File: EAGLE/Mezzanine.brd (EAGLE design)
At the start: 83 x 74 mm, 11 parts, among them U1 QBA-07+, U2 QBA-07+, U3 QBA-07+

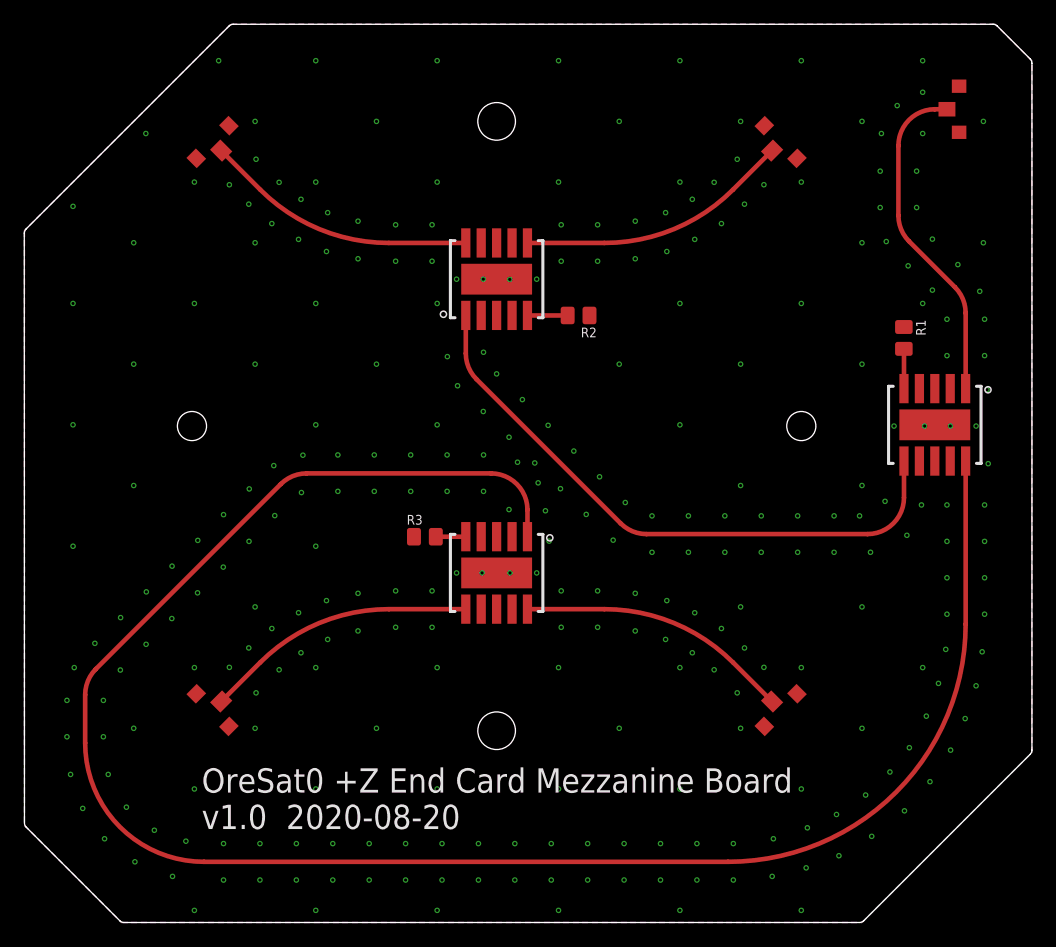
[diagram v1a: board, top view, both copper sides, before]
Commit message: Update mezzanine board to slide in past nubs
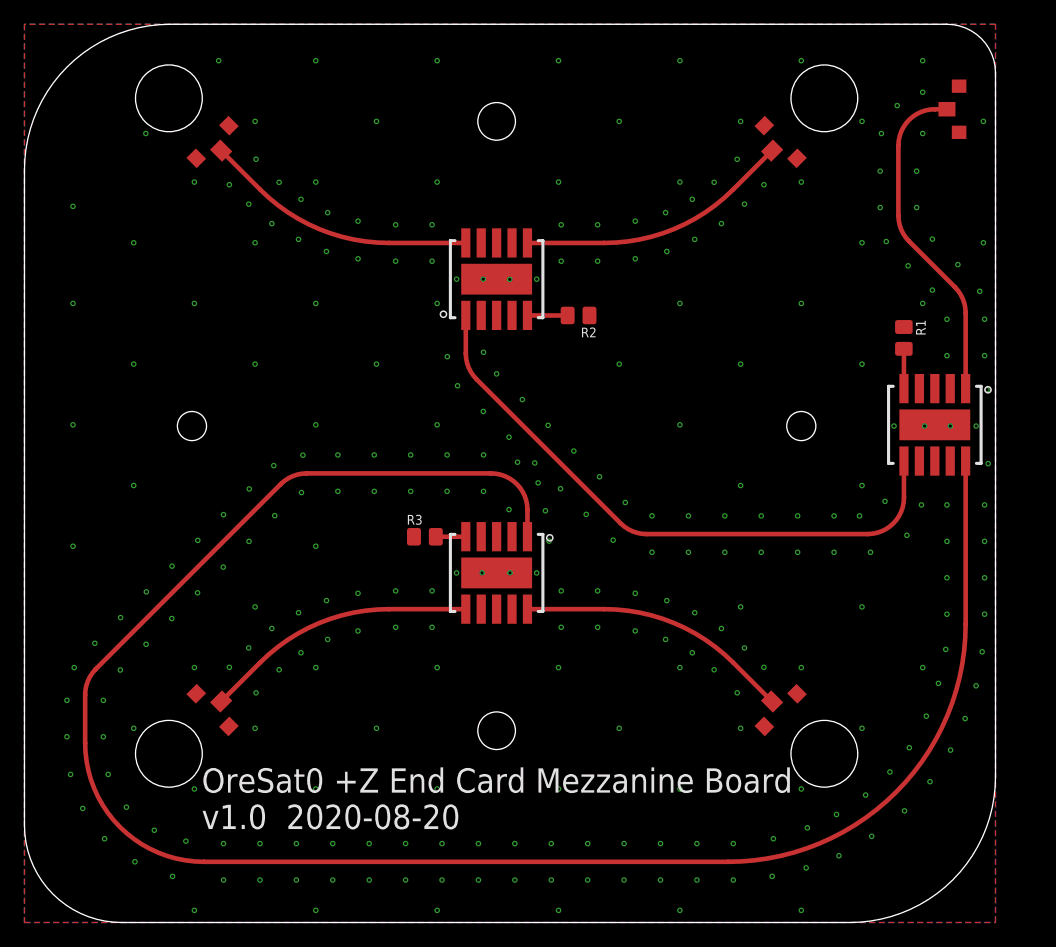
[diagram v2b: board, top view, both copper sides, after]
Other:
- board size 83 x 74 mm -> 80 x 74 mm
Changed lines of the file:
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@@
 <?xml version="1.0" encoding="utf-8"?>
 <!DOCTYPE eagle SYSTEM "eagle.dtd">
-<eagle version="9.6.1">
+<eagle version="9.6.2">
 <drawing>
 <settings>
@@
 <setting verticaltext="up"/>
 </settings>
-<grid distance="0.1" unitdist="mm" unit="mm" style="lines" multiple="1" display="yes" altdistance="0.1" altunitdist="mm" altunit="mm"/>
+<grid distance="1" unitdist="mm" unit="mm" style="lines" multiple="1" display="yes" altdistance="0.1" altunitdist="mm" altunit="mm"/>
 <layers>
-<layer number="1" name="Top" color="4" fill="1" visible="no" active="yes"/>
-<layer number="2" name="Route2" color="16" fill="1" visible="no" active="yes"/>
+<layer number="1" name="Top" color="4" fill="1" visible="yes" active="yes"/>
+<layer number="2" name="Route2" color="16" fill="1" visible="yes" active="yes"/>
 <layer number="3" name="Route3" color="17" fill="1" visible="no" active="no"/>
 <layer number="4" name="Route4" color="18" fill="1" visible="no" active="no"/>
@@
 <layer number="13" name="Route13" color="21" fill="1" visible="no" active="no"/>
 <layer number="14" name="Route14" color="22" fill="1" visible="no" active="no"/>
-<layer number="15" name="Route15" color="23" fill="1" visible="no" active="yes"/>
-<layer number="16" name="Bottom" color="1" fill="1" visible="no" active="yes"/>
-<layer number="17" name="Pads" color="2" fill="1" visible="no" active="yes"/>
-<layer number="18" name="Vias" color="2" fill="1" visible="no" active="yes"/>
-<layer number="19" name="Unrouted" color="6" fill="1" visible="no" active="yes"/>
-<layer number="20" name="Dimension" color="24" fill="1" visible="no" active="yes"/>
+<layer number="15" name="Route15" color="23" fill="1" visible="yes" active="yes"/>
+<layer number="16" name="Bottom" color="1" fill="1" visible="yes" active="yes"/>
+<layer number="17" name="Pads" color="2" fill="1" visible="yes" active="yes"/>
+<layer number="18" name="Vias" color="2" fill="1" visible="yes" active="yes"/>
+<layer number="19" name="Unrouted" color="6" fill="1" visible="yes" active="yes"/>
+<layer number="20" name="Dimension" color="24" fill="1" visible="yes" active="yes"/>
 <layer number="21" name="tPlace" color="7" fill="1" visible="no" active="yes"/>
 <layer number="22" name="bPlace" color="7" fill="1" visible="no" active="yes"/>
@@
 <layer number="43" name="vRestrict" color="2" fill="10" visible="no" active="yes"/>
 <layer number="44" name="Drills" color="7" fill="1" visible="no" active="yes"/>
-<layer number="45" name="Holes" color="7" fill="1" visible="no" active="yes"/>
+<layer number="45" name="Holes" color="7" fill="1" visible="yes" active="yes"/>
 <layer number="46" name="Milling" color="3" fill="1" visible="no" active="yes"/>
 <layer number="47" name="Measures" color="7" fill="1" visible="no" active="yes"/>
 <layer number="48" name="Document" color="7" fill="1" visible="no" active="yes"/>
 <layer number="49" name="Reference" color="7" fill="1" visible="no" active="yes"/>
-<layer number="50" name="dxf" color="11" fill="1" visible="no" active="no"/>
+<layer number="50" name="dxf" color="11" fill="1" visible="yes" active="yes"/>
 <layer number="51" name="tDocu" color="7" fill="1" visible="no" active="yes"/>
 <layer number="52" name="bDocu" color="7" fill="1" visible="no" active="yes"/>
@@
 <plain>
 <wire x1="55.75" y1="59.015" x2="55.75" y2="59.01" width="1.58" layer="29"/>
-<wire x1="28.20710625" y1="83" x2="90.79289375" y2="83" width="0.001" layer="20"/>
-<wire x1="90.79289375" y1="83" x2="91.146446875" y2="82.853553125" width="0.001" layer="20" curve="-45"/>
-<wire x1="91.146446875" y1="82.853553125" x2="93.853553125" y2="80.146446875" width="0.001" layer="20"/>
-<wire x1="93.853553125" y1="80.146446875" x2="94" y2="79.79289375" width="0.001" layer="20" curve="-45"/>
-<wire x1="94" y1="79.79289375" x2="94" y2="23.20710625" width="0.001" layer="20"/>
-<wire x1="94" y1="23.20710625" x2="93.853553125" y2="22.853553125" width="0.001" layer="20" curve="-45"/>
-<wire x1="93.853553125" y1="22.853553125" x2="80.146446875" y2="9.146446875" width="0.001" layer="20"/>
-<wire x1="80.146446875" y1="9.146446875" x2="79.79289375" y2="9" width="0.001" layer="20" curve="-45"/>
-<wire x1="79.79289375" y1="9" x2="19.20710625" y2="9" width="0.001" layer="20"/>
-<wire x1="19.20710625" y1="9" x2="18.853553125" y2="9.146446875" width="0.001" layer="20" curve="-45"/>
-<wire x1="18.853553125" y1="9.146446875" x2="11.146384375" y2="16.853615625" width="0.001" layer="20"/>
-<wire x1="11.146384375" y1="16.853615625" x2="10.9999375" y2="17.20543125" width="0.001" layer="20" curve="-44.800898"/>
-<wire x1="10.9999375" y1="17.20543125" x2="10.985159375" y2="65.779665625" width="0.001" layer="20"/>
-<wire x1="10.985159375" y1="65.779665625" x2="11.13160625" y2="66.13160625" width="0.001" layer="20" curve="-44.874123"/>
-<wire x1="11.13160625" y1="66.13160625" x2="27.853553125" y2="82.853553125" width="0.001" layer="20"/>
-<wire x1="27.853553125" y1="82.853553125" x2="28.20710625" y2="83" width="0.001" layer="20" curve="-45"/>
+<wire x1="23" y1="83" x2="87" y2="83" width="0.001" layer="20"/>
+<wire x1="87" y1="83" x2="91" y2="79" width="0.001" layer="20" curve="-90"/>
+<wire x1="91" y1="79" x2="91" y2="21" width="0.001" layer="20"/>
+<wire x1="91" y1="21" x2="79" y2="9" width="0.001" layer="20" curve="-90"/>
+<wire x1="79" y1="9" x2="19" y2="9" width="0.001" layer="20"/>
+<wire x1="19" y1="9" x2="11" y2="17" width="0.001" layer="20" curve="-90"/>
+<wire x1="11" y1="17" x2="11" y2="71" width="0.001" layer="20"/>
+<wire x1="11" y1="71" x2="23" y2="83" width="0.001" layer="20" curve="-90"/>
 <wire x1="84.6" y1="75.7" x2="83" y2="73" width="2" layer="29" curve="70"/>
 <wire x1="83" y1="73" x2="83" y2="67.242640625" width="2" layer="29"/>
@@
 <text x="74.7" y="16.7" size="2" layer="22" font="vector" ratio="10" rot="MR0">OreSat0 +Z End Card Mezzanine Board
 v1.0  2020-08-20</text>
+<circle x="22.86926875" y="76.93073125" radius="2.78" width="0.001" layer="50"/>
+<circle x="76.93073125" y="76.93073125" radius="2.78" width="0.001" layer="50"/>
+<circle x="22.86926875" y="22.86926875" radius="2.78" width="0.001" layer="50"/>
+<circle x="76.93073125" y="22.86926875" radius="2.78" width="0.001" layer="50"/>
+<wire x1="74.431359375" y1="72.16861875" x2="72.16861875" y2="74.431359375" width="0.001" layer="50"/>
+<wire x1="87.999990625" y1="77.599990625" x2="87.999990625" y2="74.399990625" width="0.001" layer="50"/>
+<wire x1="72.16861875" y1="25.368640625" x2="74.431359375" y2="27.63138125" width="0.001" layer="50"/>
+<wire x1="49.9" y1="49.9" x2="73.299990625" y2="73.299990625" width="0.001" layer="50"/>
+<wire x1="25.368640625" y1="27.63138125" x2="27.63138125" y2="25.368640625" width="0.001" layer="50"/>
+<wire x1="27.63138125" y1="74.431359375" x2="25.368640625" y2="72.16861875" width="0.001" layer="50"/>
+<wire x1="8.4" y1="87.78281875" x2="8.4" y2="3.407140625" width="0.001" layer="50"/>
+<wire x1="91.4" y1="12.9" x2="91.4" y2="8.4" width="0.001" layer="50"/>
+<wire x1="91.4" y1="87.78281875" x2="91.4" y2="3.407140625" width="0.001" layer="50"/>
+<circle x="24.799990625" y="49.899990625" radius="1.2" width="0.001" layer="50"/>
+<circle x="49.899990625" y="24.799990625" radius="1.55" width="0.001" layer="50"/>
+<circle x="74.999990625" y="49.899990625" radius="1.2" width="0.001" layer="50"/>
+<circle x="49.899990625" y="74.999990625" radius="1.55" width="0.001" layer="50"/>
+<wire x1="91" y1="21" x2="91" y2="79" width="0.001" layer="50"/>
+<wire x1="91" y1="79" x2="87" y2="83" width="0.001" layer="50" curve="90"/>
+<wire x1="87" y1="83" x2="23" y2="83" width="0.001" layer="50"/>
+<wire x1="23" y1="83" x2="11" y2="71" width="0.001" layer="50" curve="90"/>
+<wire x1="11" y1="71" x2="11" y2="17" width="0.001" layer="50"/>
+<wire x1="11" y1="17" x2="19" y2="9" width="0.001" layer="50" curve="90"/>
+<wire x1="19" y1="9" x2="79" y2="9" width="0.001" layer="50"/>
+<wire x1="79" y1="9" x2="91" y2="21" width="0.001" layer="50" curve="90"/>
+<hole x="76.9" y="76.9" drill="5.5"/>
+<hole x="22.9" y="76.9" drill="5.5"/>
+<hole x="76.9" y="22.9" drill="5.5"/>
+<hole x="22.9" y="22.9" drill="5.5"/>
 </plain>
 <attributes>
@@
 <contactref element="U$5" pad="P$2"/>
 <polygon width="0.38" layer="1" isolate="0.2" thermals="no" rank="6">
-<vertex x="11" y="66"/>
-<vertex x="11" y="17"/>
-<vertex x="19" y="9"/>
-<vertex x="80" y="9"/>
-<vertex x="94" y="23"/>
-<vertex x="94" y="80"/>
+<vertex x="11" y="83"/>
+<vertex x="11" y="9"/>
+<vertex x="91" y="9"/>
 <vertex x="91" y="83"/>
-<vertex x="28" y="83"/>
 </polygon>
 <via x="85" y="74" extent="1-16" drill="0.254"/>
@@
 <via x="71.92" y="30.02" extent="1-16" drill="0.254"/>
 <polygon width="0.38" layer="2" isolate="0.2" thermals="no" rank="6">
-<vertex x="11" y="66"/>
-<vertex x="11" y="17"/>
-<vertex x="19" y="9"/>
-<vertex x="80" y="9"/>
-<vertex x="94" y="23"/>
-<vertex x="94" y="80"/>
-<vertex x="91" y="83"/>
-<vertex x="28" y="83"/>
+<vertex x="11" y="83"/>
+<vertex x="11" y="9"/>
+<vertex x="94" y="9"/>
+<vertex x="94" y="83"/>
 </polygon>
 <polygon width="0.38" layer="15" isolate="0.2" thermals="no" rank="6">
-<vertex x="11" y="66"/>
-<vertex x="11" y="17"/>
-<vertex x="19" y="9"/>
-<vertex x="80" y="9"/>
-<vertex x="94" y="23"/>
-<vertex x="94" y="80"/>
-<vertex x="91" y="83"/>
-<vertex x="28" y="83"/>
+<vertex x="11" y="83"/>
+<vertex x="11" y="9"/>
+<vertex x="94" y="9"/>
+<vertex x="94" y="83"/>
 </polygon>
 <polygon width="0.38" layer="16" isolate="0.2" thermals="no" rank="6">
-<vertex x="11" y="66"/>
-<vertex x="11" y="17"/>
-<vertex x="19" y="9"/>
-<vertex x="80" y="9"/>
-<vertex x="94" y="23"/>
-<vertex x="94" y="80"/>
+<vertex x="11" y="83"/>
+<vertex x="11" y="9"/>
+<vertex x="91" y="9"/>
 <vertex x="91" y="83"/>
-<vertex x="28" y="83"/>
 </polygon>
 <via x="84.9" y="43.4" extent="1-16" drill="0.254"/>
